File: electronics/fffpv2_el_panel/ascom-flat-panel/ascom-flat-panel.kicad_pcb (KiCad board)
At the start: 2 copper layers, 55 x 46.9 mm, 16 parts, among them J1 Conn_01x02, J2 Servo, Q1 TIP120, Q2 IRLZ34N, U1 TLC272, U2 XIAO-SAMD21-DIP

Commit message: Missing wiring the EL driver +
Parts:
- moved J1 3.61 mm to (137.5, 106.5), turned to -90 degrees
- moved R1 1.50 mm to (146.5, 90.1)
- moved C2 1.25 mm to (145.0, 109.2)
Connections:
- Q1 pad 3: Net-(Q1-E) -> EL_DRIVER+
- R1 pad 1: Net-(Q1-E) -> EL_DRIVER+
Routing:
- net EL_DRIVER+: track 0.00 -> 22.9 mm
- net Net-(Q1-E): track 11.9 -> 0.00 mm
- net DAC_PANEL_POWER_CONTROL: track 28.0 -> 26.3 mm
- net Net-(U1A--): track 19.9 -> 19.4 mm

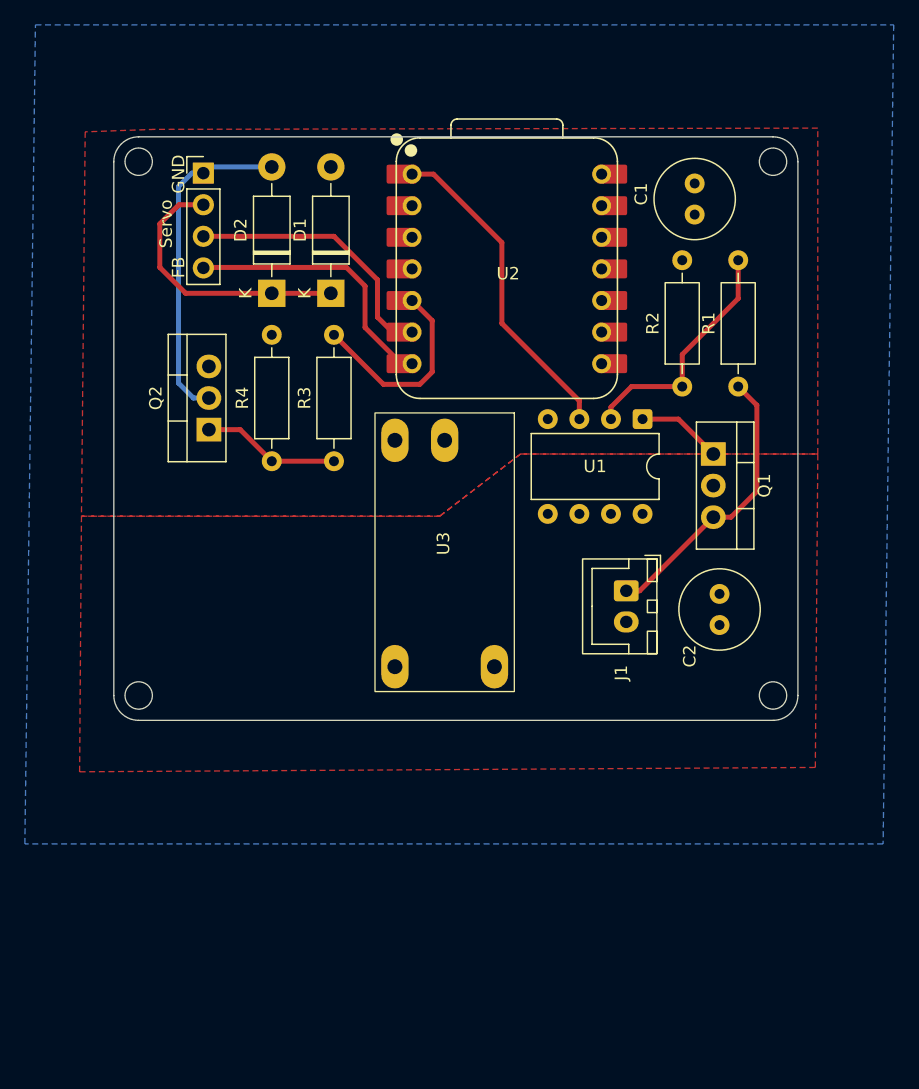
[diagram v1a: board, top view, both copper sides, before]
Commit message: Adding inverter footprint on the PCB
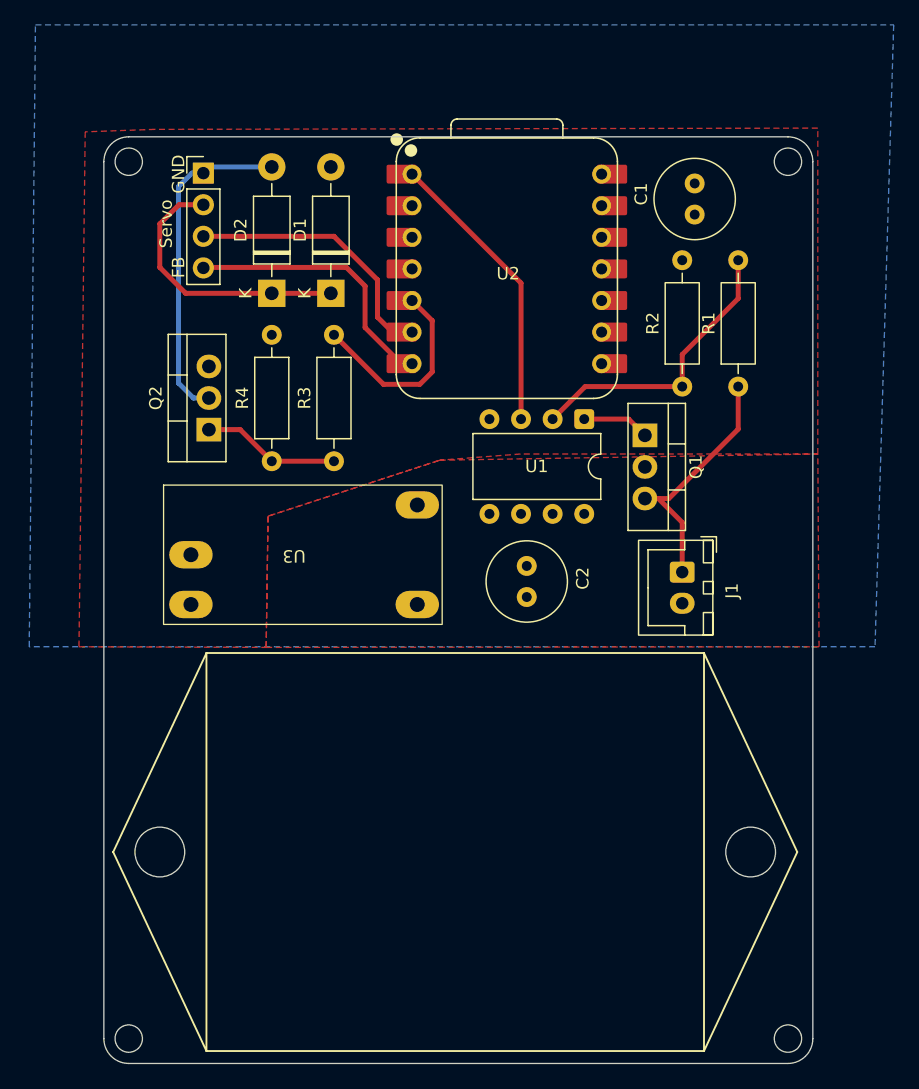
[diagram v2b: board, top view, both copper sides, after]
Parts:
- moved C2 16.2 mm to (129.5, 104.5), turned to -90 degrees
- moved U3 11.5 mm to (111.5, 103.5), turned to 0 degrees
- moved Q1 5.70 mm to (139.0, 94.0)
- moved J1 4.74 mm to (142.0, 105.0)
- moved U1 4.69 mm to (134.1, 92.7)
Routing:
- net Net-(U1A--): track 19.4 -> 23.5 mm
- net DAC_PANEL_POWER_CONTROL: track 26.3 -> 23.3 mm
- net EL_DRIVER+: track 22.9 -> 21.0 mm
- net Net-(Q1-B): track 6.85 -> 5.42 mm
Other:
- board size 55 x 46.9 mm -> 57 x 74.5 mm
